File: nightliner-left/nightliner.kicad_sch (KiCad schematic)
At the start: 86 parts, among them J1 TYPE-C-31-M-12, J2 Battery, J3 Serial, J4 Battery, P1 ISP_Prog, SW1 pinky_top, SW10 inner_home, SW11 pinky_bottom, SW12 ring_bottom, SW13 middle_bottom, SW14 index_bottom, SW15 inner_bottom, SW16 outer_top, SW17 outer_home, SW18 near_thumb, SW19 home_thumb, SW2 ring_top, SW20 far_thumb, SW21 ON_OFF, SW22 RESET, SW3 middle_top, SW4 index_top, SW5 inner_top, SW6 pinky_home, SW7 ring_home, SW8 middle_home, SW9 index_home, U1 holyiot-18010, U2 TVS2200DRV, U3 USBLC6-2SC6, U4 BQ24075RGT, U5 XC6220B331MR

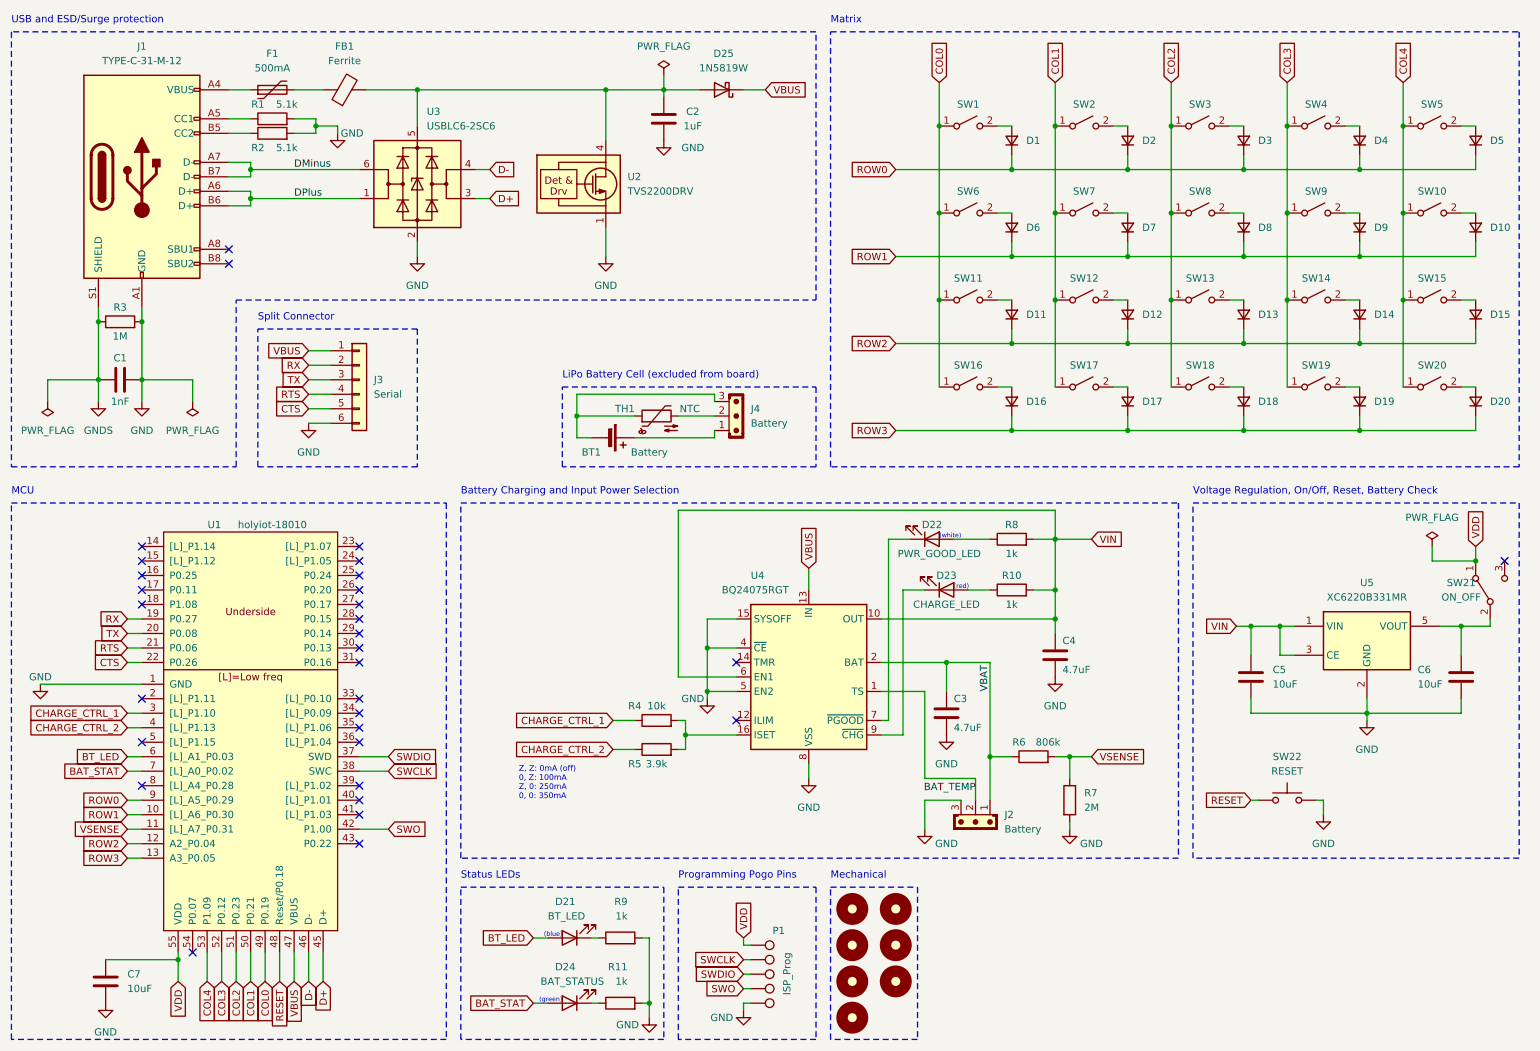
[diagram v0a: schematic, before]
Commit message: fix: make sides symmetric
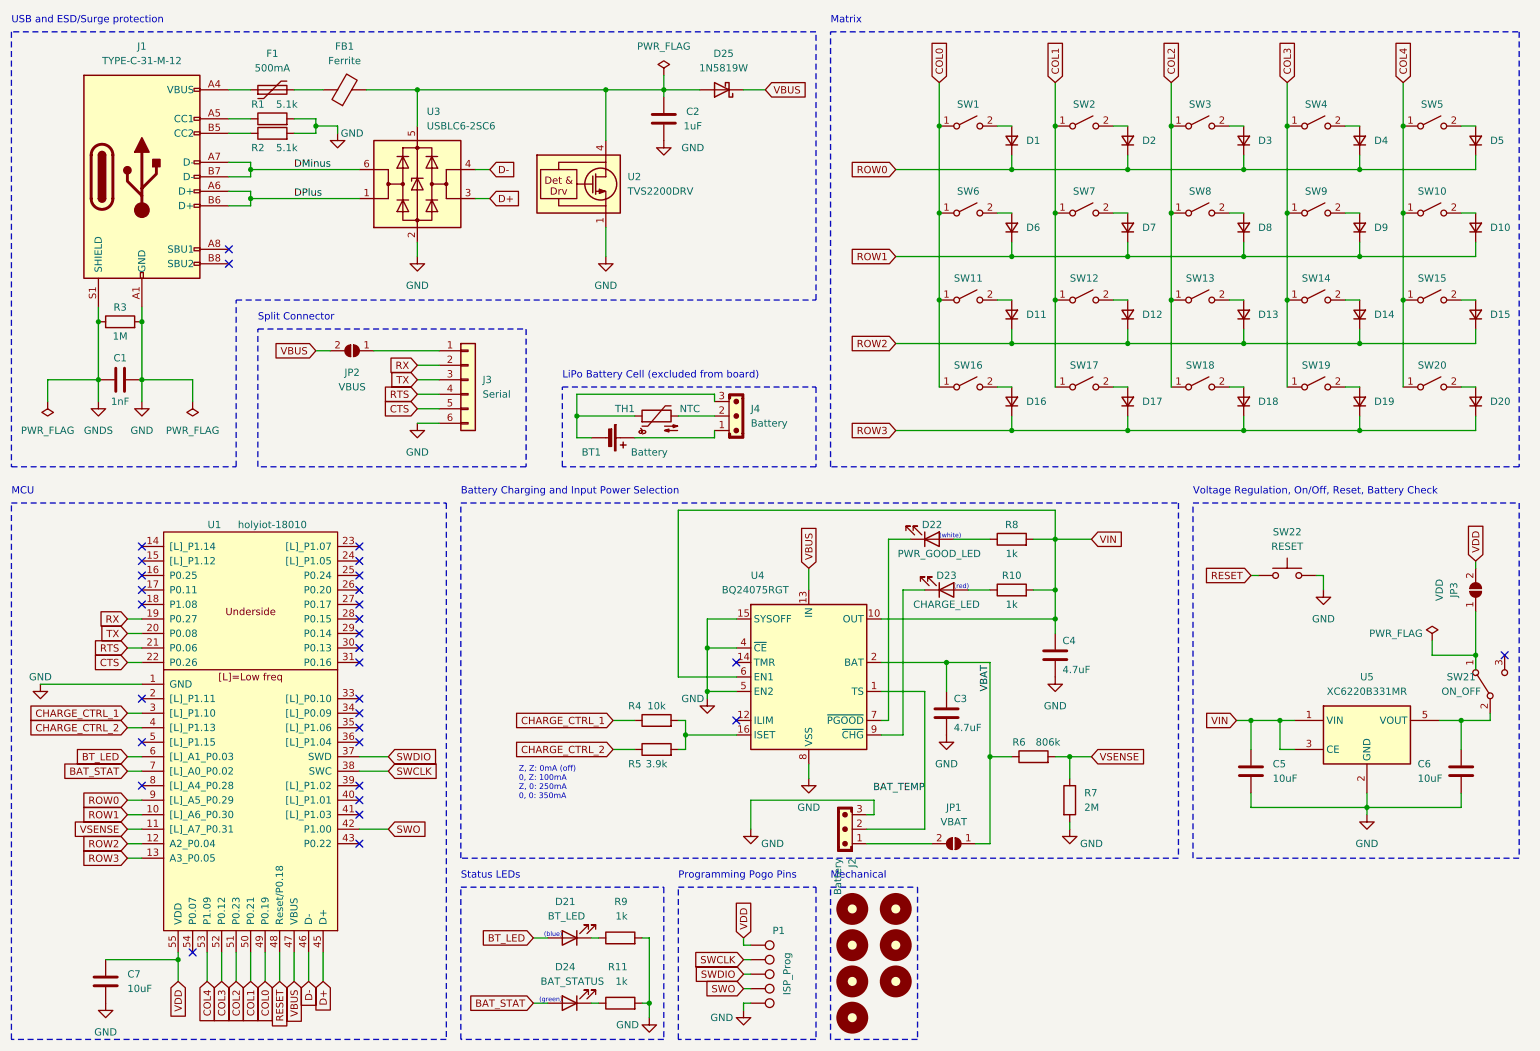
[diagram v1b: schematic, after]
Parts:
- added JP1: VBAT, Jumper:SolderJumper-2_P1.3mm_Open_RoundedPad1.0x1.5mm, symbol Jumper:SolderJumper_2_Open
- added JP2: VBUS, Jumper:SolderJumper-2_P1.3mm_Open_RoundedPad1.0x1.5mm, symbol Jumper:SolderJumper_2_Open
- added JP3: VDD, Jumper:SolderJumper-2_P1.3mm_Open_RoundedPad1.0x1.5mm, symbol Jumper:SolderJumper_2_Open
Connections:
- net VBAT: now also JP1.1 (A); no longer J2.1
- net VBUS: now also JP2.2 (B); no longer J3.1 (Pin_1)
- net VDD: now also JP3.2 (B); no longer SW21.1 (A)
- new net: JP3.1 (A), SW21.1 (A)
- new net: J2.1, JP1.2 (B)
- new net: J3.1 (Pin_1), JP2.1 (A)
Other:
- moved on the sheet: C5, C6, J2, J3, SW21, SW22, U5

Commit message: fix: change edge outline, flip switches
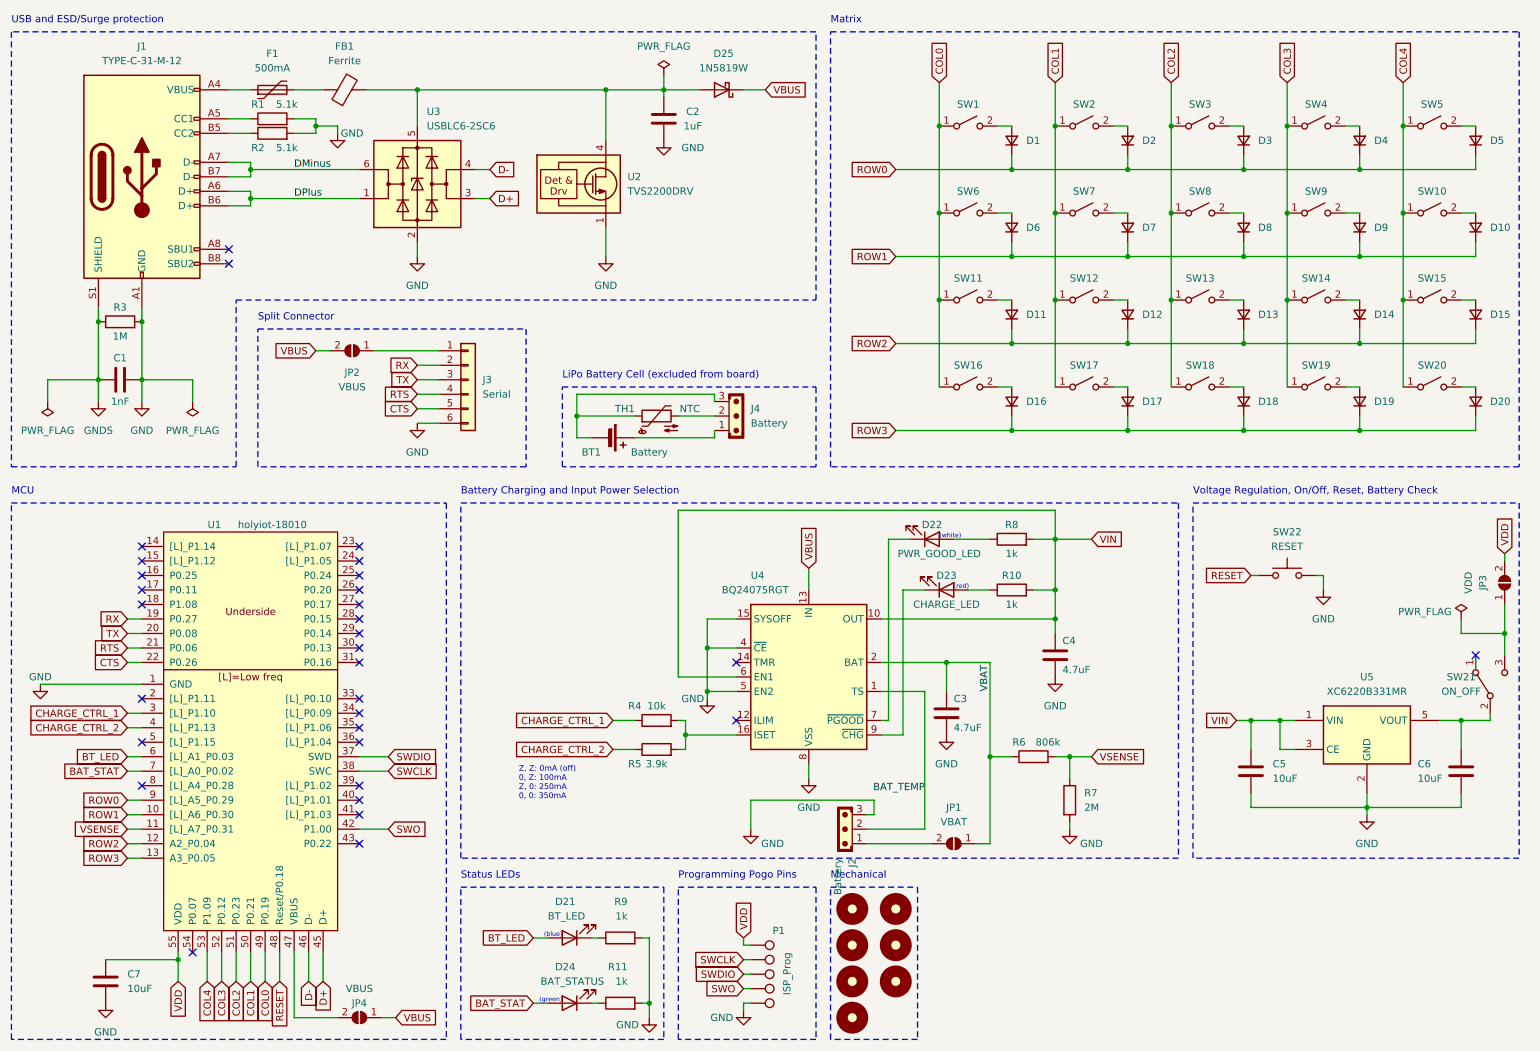
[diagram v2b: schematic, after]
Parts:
- added JP4: VBUS, Jumper:SolderJumper-2_P1.3mm_Open_RoundedPad1.0x1.5mm, symbol Jumper:SolderJumper_2_Open
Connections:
- net VBUS: now also JP4.1 (A); no longer U1.47 (VBUS)
- net at SW21.1 (A): no longer JP3.1 (A)
- net at SW21.3 (C): now also JP3.1 (A)
- new net: JP4.2 (B), U1.47 (VBUS)
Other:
- moved on the sheet: JP3
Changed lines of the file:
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@@
   (junction (at 179.07 64.77) (diameter 0) (color 0 0 0 0)
   )
-  (junction (at 273.05 127) (diameter 0) (color 0 0 0 0)
-  )
   (junction (at 212.09 72.39) (diameter 0) (color 0 0 0 0)
   )
@@
   (junction (at 199.39 120.65) (diameter 0) (color 0 0 0 0)
   )
+  (junction (at 278.13 123.19) (diameter 0) (color 0 0 0 0)
+  )
   (junction (at 39.37 68.58) (diameter 0) (color 0 0 0 0)
   )
@@
   (no_connect (at 77.47 120.65))
   (no_connect (at 77.47 118.11))
-  (no_connect (at 278.13 127))
+  (no_connect (at 273.05 127))
   (no_connect (at 39.37 118.11))
   (no_connect (at 39.37 134.62))
@@
     (stroke (width 0) (type default))
   )
-  (wire (pts (xy 273.05 119.38) (xy 273.05 127))
+  (wire (pts (xy 278.13 118.11) (xy 278.13 123.19))
     (stroke (width 0) (type default))
   )
@@
     (stroke (width 0) (type default))
   )
-  (wire (pts (xy 265.43 127) (xy 273.05 127))
+  (wire (pts (xy 270.51 123.19) (xy 278.13 123.19))
     (stroke (width 0) (type default))
   )
@@
     (stroke (width 0) (type default))
   )
+  (wire (pts (xy 73.66 190.5) (xy 66.04 190.5))
+    (stroke (width 0) (type default))
+  )
   (wire (pts (xy 58.42 46.99) (xy 77.47 46.99))
     (stroke (width 0) (type default))
@@
     (stroke (width 0) (type default))
   )
-  (wire (pts (xy 273.05 110.49) (xy 273.05 111.76))
+  (wire (pts (xy 278.13 109.22) (xy 278.13 110.49))
     (stroke (width 0) (type default))
   )
@@
     (stroke (width 0) (type default))
   )
-  (wire (pts (xy 265.43 124.46) (xy 265.43 127))
+  (wire (pts (xy 270.51 120.65) (xy 270.51 123.19))
     (stroke (width 0) (type default))
   )
@@
     (stroke (width 0) (type default))
   )
+  (wire (pts (xy 81.28 190.5) (xy 83.82 190.5))
+    (stroke (width 0) (type default))
+  )
   (wire (pts (xy 138.43 125.73) (xy 143.51 125.73))
     (stroke (width 0) (type default))
@@
     (stroke (width 0) (type default))
   )
+  (wire (pts (xy 278.13 123.19) (xy 278.13 127))
+    (stroke (width 0) (type default))
+  )
   (wire (pts (xy 246.38 113.03) (xy 245.11 113.03))
     (stroke (width 0) (type default))
   )
-  (wire (pts (xy 66.04 179.07) (xy 66.04 184.15))
+  (wire (pts (xy 66.04 179.07) (xy 66.04 190.5))
     (stroke (width 0) (type default))
   )
@@
     )
   )
-  (global_label "VBUS" (shape input) (at 66.04 184.15 270) (fields_autoplaced)
-    (effects (font (size 1.27 1.27)) (justify right))
-    (property "Intersheetrefs" "${INTERSHEET_REFS}" (at 66.04 192.0338 90)
-      (effects (font (size 1.27 1.27)) (justify right) hide)
+  (global_label "VBUS" (shape input) (at 83.82 190.5 0) (fields_autoplaced)
+    (effects (font (size 1.27 1.27)) (justify left))
+    (property "Intersheetrefs" "${INTERSHEET_REFS}" (at 91.7038 190.5 0)
+      (effects (font (size 1.27 1.27)) (justify left) hide)
     )
   )
-  (global_label "VDD" (shape input) (at 273.05 110.49 90) (fields_autoplaced)
+  (global_label "VDD" (shape input) (at 278.13 109.22 90) (fields_autoplaced)
     (effects (font (size 1.27 1.27)) (justify left))
-    (property "Intersheetrefs" "${INTERSHEET_REFS}" (at 273.05 103.8762 90)
+    (property "Intersheetrefs" "${INTERSHEET_REFS}" (at 278.13 102.6062 90)
       (effects (font (size 1.27 1.27)) (justify left) hide)
     )
@@
     )
   )
-  (symbol (lib_id "Jumper:SolderJumper_2_Open") (at 273.05 115.57 90) (unit 1)
+  (symbol (lib_id "Jumper:SolderJumper_2_Open") (at 278.13 114.3 90) (unit 1)
     (in_bom yes) (on_board yes) (dnp no)
-    (property "Reference" "JP3" (at 269.24 115.57 0)
+    (property "Reference" "JP3" (at 274.32 114.3 0)
       (effects (font (size 1.27 1.27)))
     )
-    (property "Value" "VDD" (at 266.7 115.57 0)
+    (property "Value" "VDD" (at 271.78 114.3 0)
       (effects (font (size 1.27 1.27)))
     )
-    (property "Footprint" "Jumper:SolderJumper-2_P1.3mm_Open_RoundedPad1.0x1.5mm" (at 273.05 115.57 0)
+    (property "Footprint" "Jumper:SolderJumper-2_P1.3mm_Open_RoundedPad1.0x1.5mm" (at 278.13 114.3 0)
       (effects (font (size 1.27 1.27)) hide)
     )
-    (property "Datasheet" "~" (at 273.05 115.57 0)
+    (property "Datasheet" "~" (at 278.13 114.3 0)
       (effects (font (size 1.27 1.27)) hide)
     )
-    (property "PartNumber" "" (at 273.05 115.57 0)
+    (property "PartNumber" "" (at 278.13 114.3 0)
       (effects (font (size 1.27 1.27)) hide)
     )
-    (property "LCSCNumber" "" (at 273.05 115.57 0)
+    (property "LCSCNumber" "" (at 278.13 114.3 0)
       (effects (font (size 1.27 1.27)) hide)
     )
@@
     )
   )
-  (symbol (lib_id "power:PWR_FLAG") (at 265.43 124.46 0) (unit 1)
+  (symbol (lib_id "power:PWR_FLAG") (at 270.51 120.65 0) (unit 1)
     (in_bom yes) (on_board yes) (dnp no)
-    (property "Reference" "#FLG03" (at 265.43 122.555 0)
+    (property "Reference" "#FLG03" (at 270.51 118.745 0)
       (effects (font (size 1.27 1.27)) hide)
     )
-    (property "Value" "PWR_FLAG" (at 259.08 123.19 0)
+    (property "Value" "PWR_FLAG" (at 264.16 119.38 0)
       (effects (font (size 1.27 1.27)))
     )
-    (property "Footprint" "" (at 265.43 124.46 0)
+    (property "Footprint" "" (at 270.51 120.65 0)
       (effects (font (size 1.27 1.27)) hide)
     )
-    (property "Datasheet" "~" (at 265.43 124.46 0)
+    (property "Datasheet" "~" (at 270.51 120.65 0)
       (effects (font (size 1.27 1.27)) hide)
     )
@@
         )
       )
+    )
+  )
+  (symbol (lib_id "Jumper:SolderJumper_2_Open") (at 77.47 190.5 180) (unit 1)
+    (in_bom yes) (on_board yes) (dnp no)
+    (property "Reference" "JP4" (at 77.47 187.96 0)
+      (effects (font (size 1.27 1.27)))
+    )
+    (property "Value" "VBUS" (at 77.47 185.42 0)
+      (effects (font (size 1.27 1.27)))
+    )
+    (property "Footprint" "Jumper:SolderJumper-2_P1.3mm_Open_RoundedPad1.0x1.5mm" (at 77.47 190.5 0)
+      (effects (font (size 1.27 1.27)) hide)
+    )
+    (property "Datasheet" "~" (at 77.47 190.5 0)
+      (effects (font (size 1.27 1.27)) hide)
+    )
+    (property "PartNumber" "" (at 77.47 190.5 0)
+      (effects (font (size 1.27 1.27)) hide)
+    )
+    (property "LCSCNumber" "" (at 77.47 190.5 0)
+      (effects (font (size 1.27 1.27)) hide)
+    )
+    (pin "1")
+    (pin "2")
+    (instances
+      (project "nightliner"
+        (path "/e4693d91-d111-4059-a601-28406aaad775"
+          (reference "JP4") (unit 1)
+        )
+      )

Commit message: fix: final version, create production gerbers
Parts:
- H1, H2, H3, H4, H5, H6, H7: footprint miro_keyboard:StandOff_6mm_M3 -> nightliner:StandOff_6mm_M3
- J1: footprint Connector_USB:USB_C_Receptacle_HRO_TYPE-C-31-M-12 -> (none); symbol Connector:USB_C_Receptacle_USB2.0 -> nightliner:USB_C_Receptacle_USB2.0
- J3: footprint miro_keyboard:MagConn_6pin_left -> nightliner:MagConn_6pin_left
- P1: footprint miro_keyboard:ISP_Programming_Pads -> nightliner:ISP_Programming_Pads; symbol miro_keyboard:ISP_Prog -> nightliner:ISP_Prog
- SW1, SW10, SW11, SW12, SW13, SW14, SW15, SW16, SW17, SW18, SW19, SW2, SW20, SW3, SW4, SW5, SW6, SW7, SW8, SW9: footprint miro_keyboard:Kailh_Choc_CPG135001D02_Hotswap -> nightliner:Kailh_Choc_CPG135001D02_Hotswap
- SW21: footprint miro_keyboard:SW_ROCPU_SK-12D07-5_SPDT_Angled -> nightliner:SW_ROCPU_SK-12D07-5_SPDT_Angled
- SW22: footprint miro_keyboard:SW_Push_1P1T_NO_CK_KSC4xxJ -> nightliner:SW_Push_1P1T_NO_CK_KSC4xxJ
- U1: footprint miro_keyboard:HOLYIOT-18010-UndersidePins-SMD -> nightliner:HOLYIOT-18010-UndersidePins-SMD
- U4: footprint miro_keyboard:VQFN-16-1EP_3x3mm_P0.5mm_EP1.6x1.6mm_ThermalVias -> nightliner:VQFN-16-1EP_3x3mm_P0.5mm_EP1.6x1.6mm_ThermalVias
